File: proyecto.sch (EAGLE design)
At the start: 42 parts, among them IC1 ADE9153AACPZ, J1 796638-3, K1 PR28-3V-360-1A-E, Q1 12.288M, Q2 BSS123, U1 ESP32-PICO-MINI-02-N8R2ESP32-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

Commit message: Errores DRC solucionados
Se revisaron los errores DRC acerca de las conexiones faltantes. Ya no hay errores DRC. Falta montar diodos led indicativos y cambiar el boton de boot de ser necesario
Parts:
- R1, R2: value 150k -> 150
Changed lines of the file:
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@@
 <part name="C18" library="rcl" library_urn="urn:adsk.eagle:library:334" deviceset="C-EU" device="C0402K" package3d_urn="urn:adsk.eagle:package:23679/2" value="0.1u"/>
 <part name="C19" library="rcl" library_urn="urn:adsk.eagle:library:334" deviceset="C-EU" device="C0402K" package3d_urn="urn:adsk.eagle:package:23679/2" value="0.1u"/>
-<part name="R1" library="rcl" library_urn="urn:adsk.eagle:library:334" deviceset="R-US_" device="R0402" package3d_urn="urn:adsk.eagle:package:23547/3" value="150k"/>
-<part name="R2" library="rcl" library_urn="urn:adsk.eagle:library:334" deviceset="R-US_" device="R0402" package3d_urn="urn:adsk.eagle:package:23547/3" value="150k"/>
+<part name="R1" library="rcl" library_urn="urn:adsk.eagle:library:334" deviceset="R-US_" device="R0402" package3d_urn="urn:adsk.eagle:package:23547/3" value="150"/>
+<part name="R2" library="rcl" library_urn="urn:adsk.eagle:library:334" deviceset="R-US_" device="R0402" package3d_urn="urn:adsk.eagle:package:23547/3" value="150"/>
 <part name="R3" library="SamacSys_Parts" deviceset="WSK12161L000FEB" device=""/>
 <part name="R4" library="rcl" library_urn="urn:adsk.eagle:library:334" deviceset="R-US_" device="R0603" package3d_urn="urn:adsk.eagle:package:23555/3" value="330k"/>
@@
 <pinref part="R8" gate="G$1" pin="1"/>
 <wire x1="218.44" y1="109.22" x2="213.36" y2="109.22" width="0.1524" layer="91"/>
-<label x="198.12" y="109.22" size="1.778" layer="95"/>
-</segment>
-<segment>
+<label x="213.36" y="109.22" size="1.778" layer="95" rot="R180" xref="yes"/>
+</segment>
+<segment>

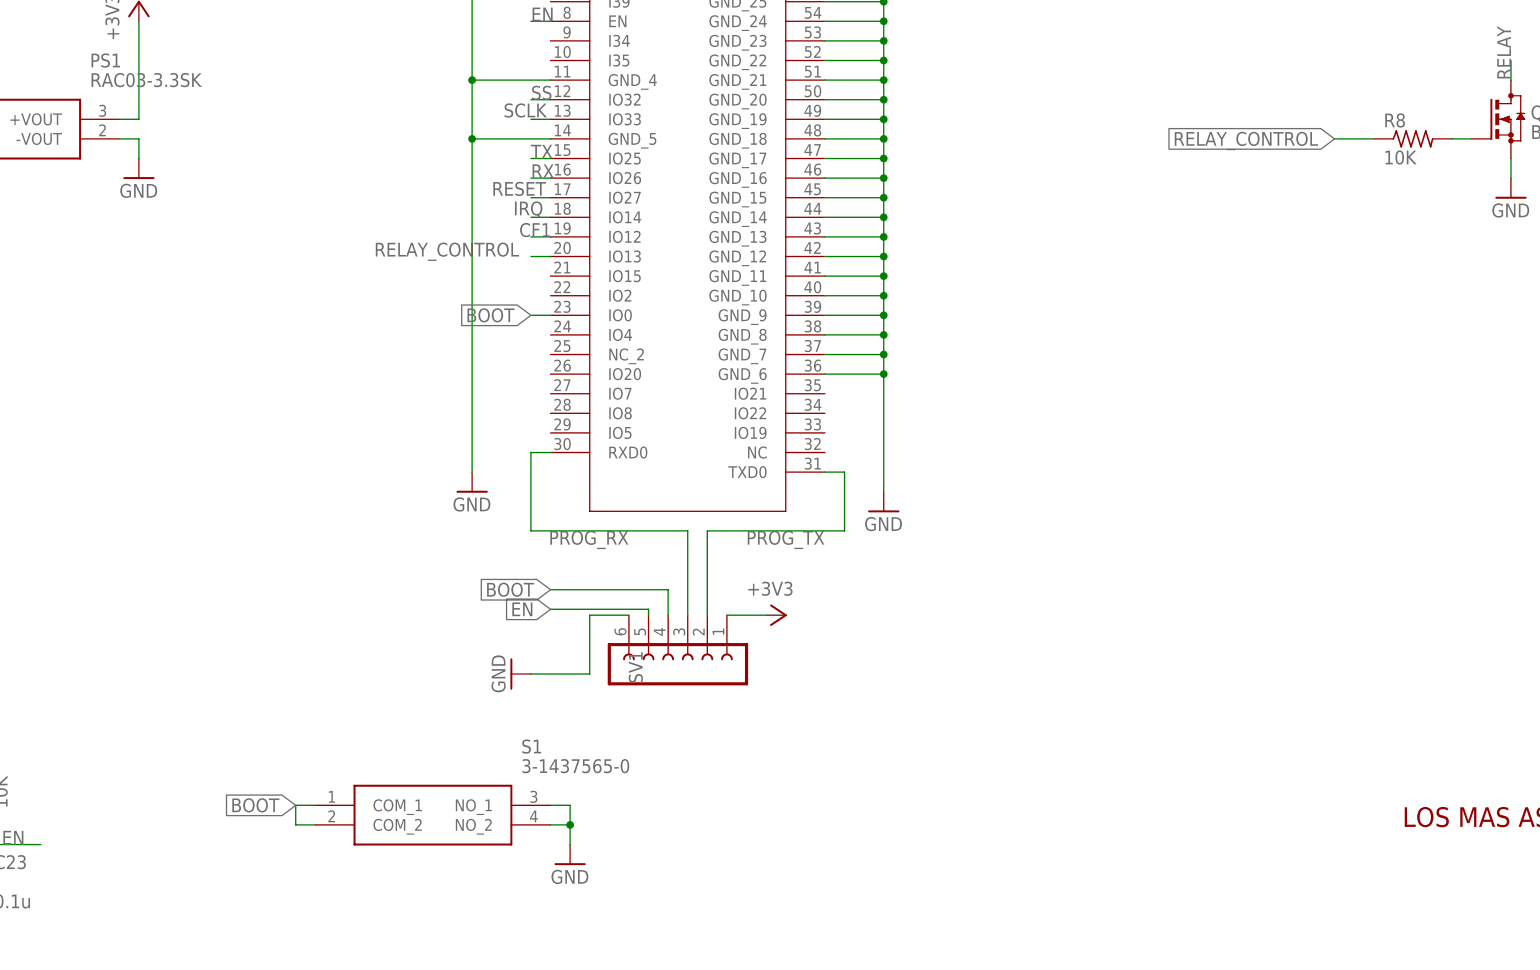
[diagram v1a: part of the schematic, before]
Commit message: Diseño terminado
Se termino el diseño del esquematico y de la PCB
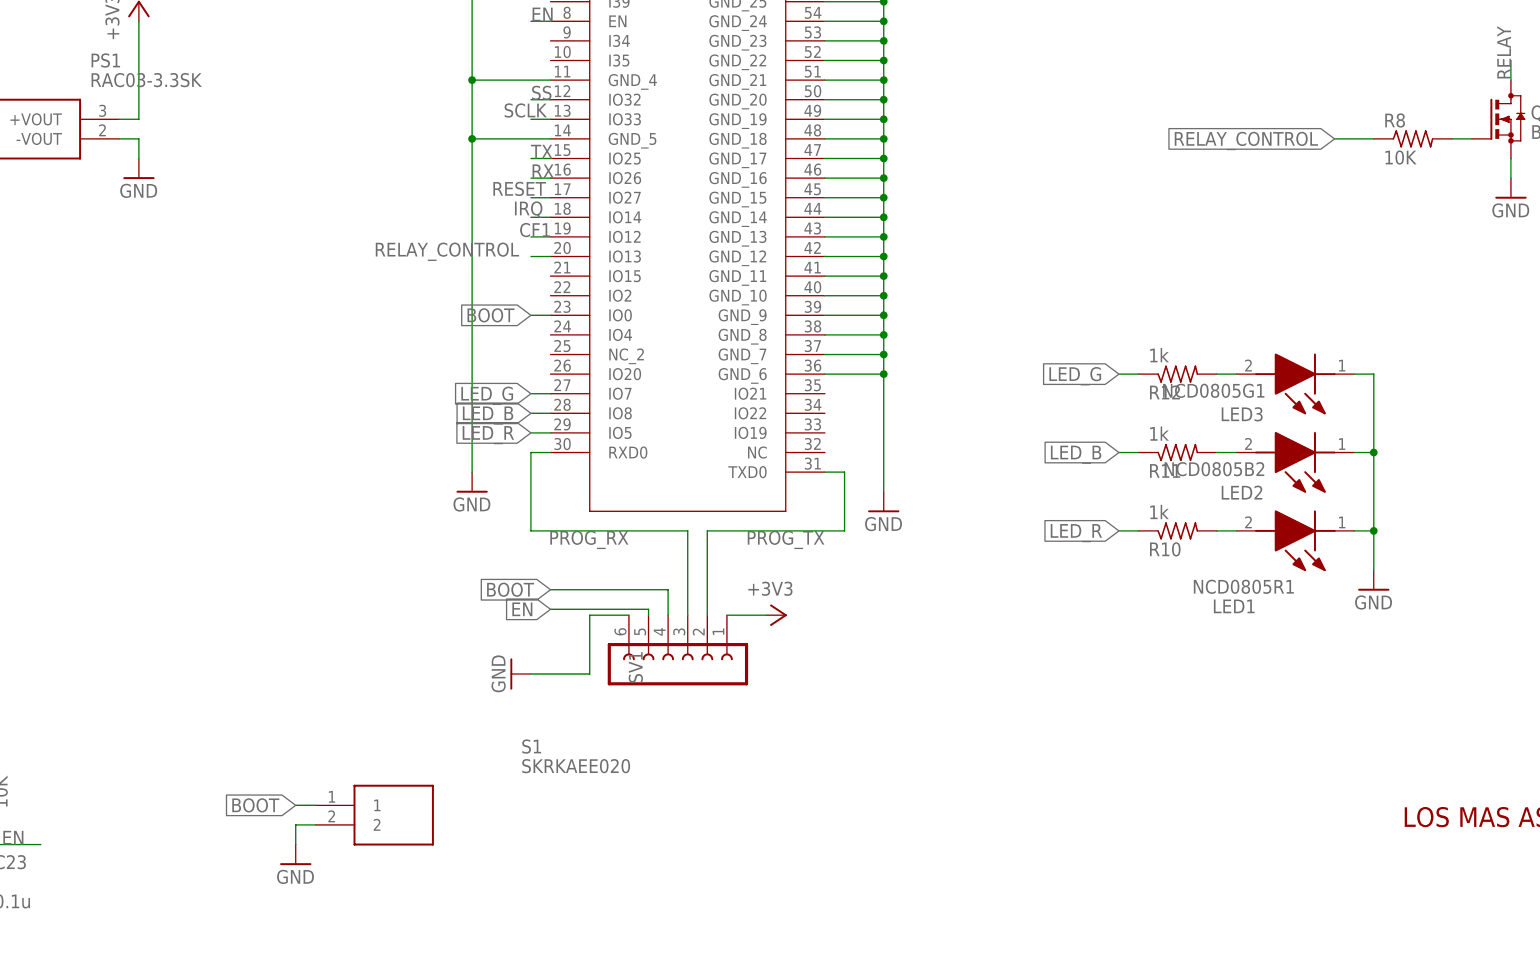
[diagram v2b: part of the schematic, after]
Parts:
- added LED1: NCD0805R1, SamacSys_Parts:NCD0805R1
- added LED2: NCD0805B2, libreria_propia:NCD0805B2
- added LED3: NCD0805G1, libreria_propia:NCD0805G1
- added R10, R11, R12: 1k, rcl:R-US_R0402
- S1: value 3-1437565-0 -> SKRKAEE020; device SamacSys_Parts:3-1437565-0 -> SamacSys_Parts:SKRKAEE020
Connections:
- new net LED_B: R11.1, U1.IO8
- new net LED_G: R12.1, U1.IO7
- new net LED_R: R10.1, U1.IO5
- new net N$11: LED1.A, R10.2
- new net N$12: LED2.A, R11.2
- new net N$14: LED3.A, R12.2
- net BOOT: now also S1.1; no longer S1.COM_1, S1.COM_2
- net GND: now also LED1.K, LED2.K, LED3.K, S1.2; no longer S1.NO_1, S1.NO_2
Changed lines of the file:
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@@
 <part name="+3V7" library="supply1" library_urn="urn:adsk.eagle:library:371" deviceset="+3V3" device=""/>
 <part name="+3V8" library="supply1" library_urn="urn:adsk.eagle:library:371" deviceset="+3V3" device=""/>
-<part name="S1" library="SamacSys_Parts" deviceset="3-1437565-0" device=""/>
+<part name="S1" library="SamacSys_Parts" deviceset="SKRKAEE020" device=""/>
 <part name="GND16" library="supply1" library_urn="urn:adsk.eagle:library:371" deviceset="GND" device=""/>
+<part name="LED1" library="SamacSys_Parts" deviceset="NCD0805R1" device=""/>
+<part name="R10" library="rcl" library_urn="urn:adsk.eagle:library:334" deviceset="R-US_" device="R0402" package3d_urn="urn:adsk.eagle:package:23547/3" value="1k"/>
+<part name="GND19" library="supply1" library_urn="urn:adsk.eagle:library:371" deviceset="GND" device=""/>
+<part name="LED2" library="libreria_propia" deviceset="NCD0805B2" device=""/>
+<part name="R11" library="rcl" library_urn="urn:adsk.eagle:library:334" deviceset="R-US_" device="R0402" package3d_urn="urn:adsk.eagle:package:23547/3" value="1k"/>
+<part name="LED3" library="libreria_propia" deviceset="NCD0805G1" device=""/>
+<part name="R12" library="rcl" library_urn="urn:adsk.eagle:library:334" deviceset="R-US_" device="R0402" package3d_urn="urn:adsk.eagle:package:23547/3" value="1k"/>
 </parts>
 <sheets>
@@
 <attribute name="VALUE" x="107.95" y="27.94" size="1.778" layer="96" align="center-left"/>
 </instance>
-<instance part="GND16" gate="1" x="114.3" y="15.24" smashed="yes">
-<attribute name="VALUE" x="111.76" y="12.7" size="1.778" layer="96"/>
+<instance part="GND16" gate="1" x="78.74" y="15.24" smashed="yes">
+<attribute name="VALUE" x="76.2" y="12.7" size="1.778" layer="96"/>
+</instance>
+<instance part="LED1" gate="G$1" x="215.9" y="58.42" smashed="yes" rot="R180">
+<attribute name="NAME" x="203.2" y="49.53" size="1.778" layer="95" rot="R180"/>
+<attribute name="VALUE" x="208.28" y="52.07" size="1.778" layer="96" rot="R180"/>
+</instance>
+<instance part="R10" gate="G$1" x="193.04" y="58.42" smashed="yes" rot="MR180">
+<attribute name="NAME" x="189.23" y="56.9214" size="1.778" layer="95" rot="MR180"/>
+<attribute name="VALUE" x="189.23" y="61.722" size="1.778" layer="96" rot="MR180"/>
+</instance>
+<instance part="GND19" gate="1" x="218.44" y="50.8" smashed="yes">
+<attribute name="VALUE" x="215.9" y="48.26" size="1.778" layer="96"/>
+</instance>
+<instance part="LED2" gate="G$1" x="215.9" y="68.58" smashed="yes" rot="R180">
+<attribute name="NAME" x="204.216" y="64.262" size="1.778" layer="95" rot="R180"/>
+<attribute name="VALUE" x="204.47" y="67.31" size="1.778" layer="96" rot="R180"/>
+</instance>
+<instance part="R11" gate="G$1" x="193.04" y="68.58" smashed="yes" rot="MR180">
+<attribute name="NAME" x="189.23" y="67.0814" size="1.778" layer="95" rot="MR180"/>
+<attribute name="VALUE" x="189.23" y="71.882" size="1.778" layer="96" rot="MR180"/>
+</instance>
+<instance part="LED3" gate="G$1" x="215.9" y="78.74" smashed="yes" rot="R180">
+<attribute name="NAME" x="204.216" y="74.422" size="1.778" layer="95" rot="R180"/>
+<attribute name="VALUE" x="204.47" y="77.47" size="1.778" layer="96" rot="R180"/>
+</instance>
+<instance part="R12" gate="G$1" x="193.04" y="78.74" smashed="yes" rot="MR180">
+<attribute name="NAME" x="189.23" y="77.2414" size="1.778" layer="95" rot="MR180"/>
+<attribute name="VALUE" x="189.23" y="82.042" size="1.778" layer="96" rot="MR180"/>
 </instance>
 </instances>
@@
 <wire x1="387.35" y1="17.272" x2="382.27" y2="17.272" width="0.1524" layer="91"/>
 <junction x="382.27" y="17.272"/>
-</segment>
-<segment>
-<pinref part="PS1" gate="G$1" pin="-VOUT"/>
-<wire x1="55.88" y1="109.22" x2="58.42" y2="109.22" width="0.1524" layer="91"/>
-<pinref part="GND12" gate="1" pin="GND"/>
-<wire x1="58.42" y1="109.22" x2="58.42" y2="106.68" width="0.1524" layer="91"/>
 </segment>
 <segment>
@@
 </segment>
 <segment>
-<pinref part="GND16" gate="1" pin="GND"/>
-<pinref part="S1" gate="G$1" pin="NO_1"/>
-<wire x1="114.3" y1="17.78" x2="114.3" y2="20.32" width="0.1524" layer="91"/>
-<wire x1="114.3" y1="20.32" x2="114.3" y2="22.86" width="0.1524" layer="91"/>
-<wire x1="114.3" y1="22.86" x2="111.76" y2="22.86" width="0.1524" layer="91"/>
-<pinref part="S1" gate="G$1" pin="NO_2"/>
-<wire x1="111.76" y1="20.32" x2="114.3" y2="20.32" width="0.1524" layer="91"/>
-<junction x="114.3" y="20.32"/>
-</segment>
-<segment>
 <pinref part="SV1" gate="G$1" pin="6"/>
 <wire x1="121.92" y1="47.498" x2="116.84" y2="47.498" width="0.1524" layer="91"/>
@@
 <pinref part="GND14" gate="1" pin="GND"/>
 <wire x1="116.84" y1="39.878" x2="109.22" y2="39.878" width="0.1524" layer="91"/>
+</segment>
+<segment>
+<pinref part="GND16" gate="1" pin="GND"/>
+<wire x1="78.74" y1="17.78" x2="78.74" y2="20.32" width="0.1524" layer="91"/>
+<pinref part="S1" gate="G$1" pin="2"/>
+<wire x1="78.74" y1="20.32" x2="81.28" y2="20.32" width="0.1524" layer="91"/>
+</segment>
+<segment>
+<pinref part="LED1" gate="G$1" pin="K"/>
+<wire x1="215.9" y1="58.42" x2="218.44" y2="58.42" width="0.1524" layer="91"/>
+<pinref part="GND19" gate="1" pin="GND"/>
+<wire x1="218.44" y1="58.42" x2="218.44" y2="53.34" width="0.1524" layer="91"/>
+<pinref part="LED2" gate="G$1" pin="K"/>
+<wire x1="215.9" y1="68.58" x2="218.44" y2="68.58" width="0.1524" layer="91"/>
+<wire x1="218.44" y1="68.58" x2="218.44" y2="58.42" width="0.1524" layer="91"/>
+<junction x="218.44" y="58.42"/>
+<pinref part="LED3" gate="G$1" pin="K"/>
+<wire x1="215.9" y1="78.74" x2="218.44" y2="78.74" width="0.1524" layer="91"/>
+<wire x1="218.44" y1="78.74" x2="218.44" y2="68.58" width="0.1524" layer="91"/>
+<junction x="218.44" y="68.58"/>
+</segment>
+<segment>
+<pinref part="PS1" gate="G$1" pin="-VOUT"/>
+<wire x1="55.88" y1="109.22" x2="58.42" y2="109.22" width="0.1524" layer="91"/>
+<pinref part="GND12" gate="1" pin="GND"/>
+<wire x1="58.42" y1="106.68" x2="58.42" y2="109.22" width="0.1524" layer="91"/>
 </segment>
 </net>
@@
 <segment>
 <pinref part="R8" gate="G$1" pin="1"/>
+<label x="213.36" y="109.22" size="1.778" layer="95" rot="R180" xref="yes"/>
 <wire x1="218.44" y1="109.22" x2="213.36" y2="109.22" width="0.1524" layer="91"/>
-<label x="213.36" y="109.22" size="1.778" layer="95" rot="R180" xref="yes"/>
 </segment>
 <segment>
@@
 <net name="BOOT" class="0">
 <segment>
-<pinref part="S1" gate="G$1" pin="COM_1"/>
+<label x="78.74" y="22.86" size="1.778" layer="95" rot="R180" xref="yes"/>
+<pinref part="S1" gate="G$1" pin="1"/>
 <wire x1="81.28" y1="22.86" x2="78.74" y2="22.86" width="0.1524" layer="91"/>
-<label x="78.74" y="22.86" size="1.778" layer="95" rot="R180" xref="yes"/>
-<pinref part="S1" gate="G$1" pin="COM_2"/>
-<wire x1="81.28" y1="20.32" x2="78.74" y2="20.32" width="0.1524" layer="91"/>
-<wire x1="78.74" y1="20.32" x2="78.74" y2="22.86" width="0.1524" layer="91"/>
 </segment>
 <segment>
@@
 </segment>
 </net>
+<net name="LED_R" class="0">
+<segment>
+<pinref part="R10" gate="G$1" pin="1"/>
+<wire x1="187.96" y1="58.42" x2="185.42" y2="58.42" width="0.1524" layer="91"/>
+<label x="185.42" y="58.42" size="1.778" layer="95" rot="R180" xref="yes"/>
+</segment>
+<segment>
+<pinref part="U1" gate="A" pin="IO5"/>
+<wire x1="111.76" y1="71.12" x2="109.22" y2="71.12" width="0.1524" layer="91"/>
+<label x="109.22" y="71.12" size="1.778" layer="95" rot="R180" xref="yes"/>
+</segment>
+</net>
+<net name="N$11" class="0">
+<segment>
+<pinref part="R10" gate="G$1" pin="2"/>
+<pinref part="LED1" gate="G$1" pin="A"/>
+<wire x1="198.12" y1="58.42" x2="200.66" y2="58.42" width="0.1524" layer="91"/>
+</segment>
+</net>
+<net name="N$12" class="0">
+<segment>
+<pinref part="R11" gate="G$1" pin="2"/>
+<pinref part="LED2" gate="G$1" pin="A"/>
+<wire x1="198.12" y1="68.58" x2="200.66" y2="68.58" width="0.1524" layer="91"/>
+</segment>
+</net>
+<net name="LED_B" class="0">
+<segment>
+<pinref part="R11" gate="G$1" pin="1"/>
+<wire x1="187.96" y1="68.58" x2="185.42" y2="68.58" width="0.1524" layer="91"/>
+<label x="185.42" y="68.58" size="1.778" layer="95" rot="R180" xref="yes"/>
+</segment>
+<segment>
+<pinref part="U1" gate="A" pin="IO8"/>
+<wire x1="111.76" y1="73.66" x2="109.22" y2="73.66" width="0.1524" layer="91"/>
+<label x="109.22" y="73.66" size="1.778" layer="95" rot="R180" xref="yes"/>
+</segment>
+</net>
+<net name="N$14" class="0">
+<segment>
+<pinref part="R12" gate="G$1" pin="2"/>
+<pinref part="LED3" gate="G$1" pin="A"/>
+<wire x1="198.12" y1="78.74" x2="200.66" y2="78.74" width="0.1524" layer="91"/>
+</segment>
+</net>
+<net name="LED_G" class="0">
+<segment>
+<pinref part="R12" gate="G$1" pin="1"/>
+<wire x1="187.96" y1="78.74" x2="185.42" y2="78.74" width="0.1524" layer="91"/>
+<label x="185.42" y="78.74" size="1.778" layer="95" rot="R180" xref="yes"/>
+</segment>
+<segment>
+<pinref part="U1" gate="A" pin="IO7"/>
+<wire x1="111.76" y1="76.2" x2="109.22" y2="76.2" width="0.1524" layer="91"/>
+<label x="109.22" y="76.2" size="1.778" layer="95" rot="R180" xref="yes"/>
+</segment>
+</net>
